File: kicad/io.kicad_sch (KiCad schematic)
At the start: 23 parts, among them J15 GPIO 5, J16 GPIO 6, J17 GPIO 20, J18 GPIO 21, J19 1-wire DS1820, J22 I2C 1, J23 I2C 2, J24 Display

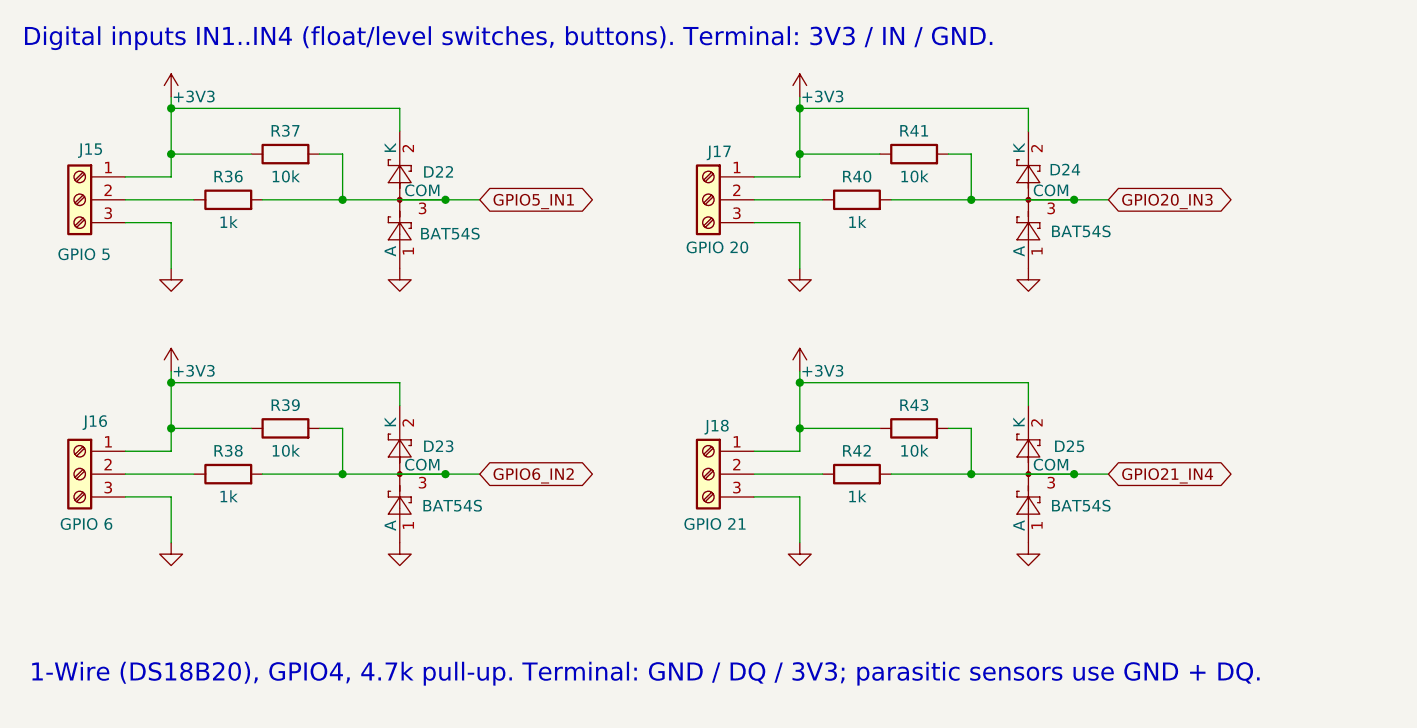
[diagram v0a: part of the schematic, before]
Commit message: kicad: strip obsolete v1 parts for v2 (SSR sheet, IN1..IN4, pH front end)
41 parts, their tracks/vias, pH guard zones, BNC keep-out and port silk removed; freed J2/U5 pins marked no-connect. ERC 0, DRC 0, parity 0; one expected +3V3 ratsnest to J24/JP3/J27/D28 left for the v2 layout.

Co-Authored-By: Claude Opus 5.5 <noreply@anthropic.com>
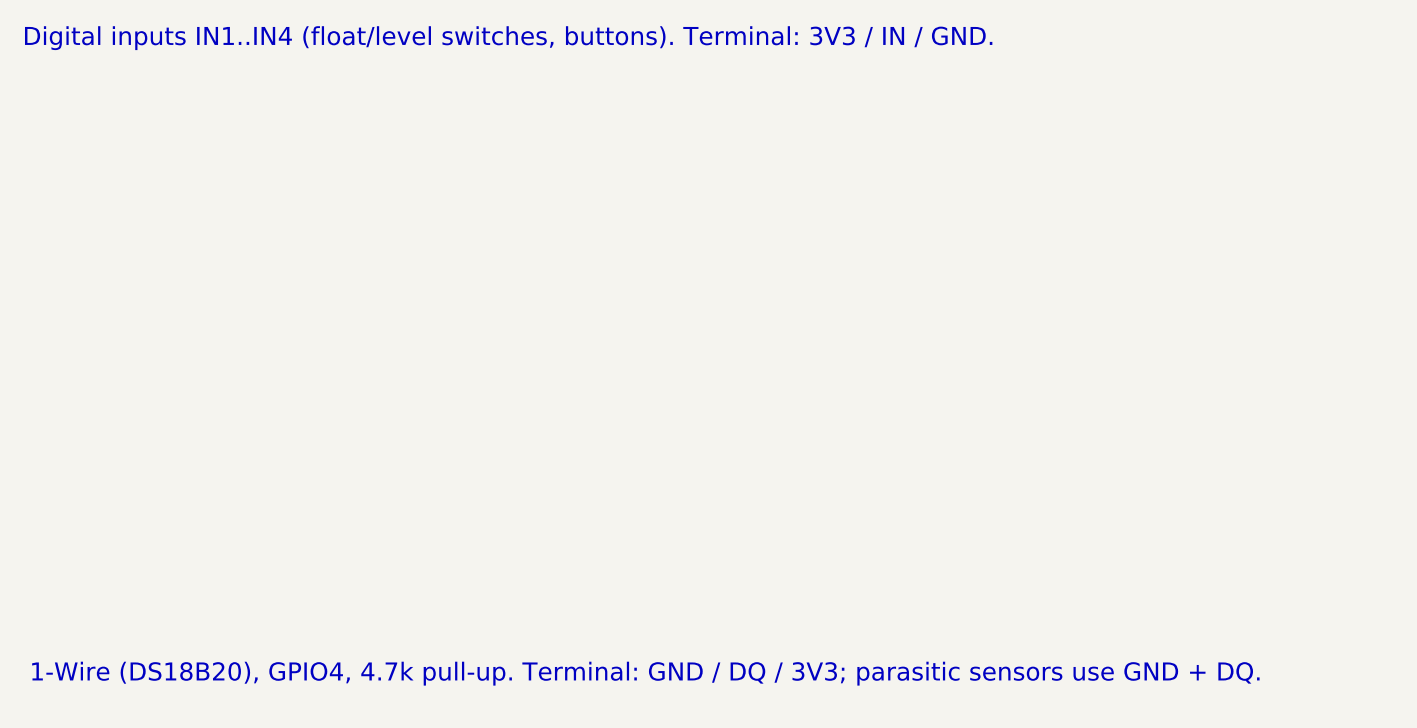
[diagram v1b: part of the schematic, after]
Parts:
- removed D22, D23, D24, D25: BAT54S, Package_TO_SOT_SMD:SOT-23, symbol Diode:BAT54S
- removed J15: GPIO 5, aquaPCB:TerminalBlock_Kangnex_WJ250B-3.5-03P_P3.50mm_Staggered, symbol Connector:Screw_Terminal_01x03
- removed J16: GPIO 6, aquaPCB:TerminalBlock_Kangnex_WJ250B-3.5-03P_P3.50mm_Staggered, symbol Connector:Screw_Terminal_01x03
- removed J17: GPIO 20, aquaPCB:TerminalBlock_Kangnex_WJ250B-3.5-03P_P3.50mm_Staggered, symbol Connector:Screw_Terminal_01x03
- removed J18: GPIO 21, aquaPCB:TerminalBlock_Kangnex_WJ250B-3.5-03P_P3.50mm_Staggered, symbol Connector:Screw_Terminal_01x03
- removed R36, R38, R40, R42: 1k, Resistor_SMD:R_0805_2012Metric, symbol Device:R
- removed R37, R39, R41, R43: 10k, Resistor_SMD:R_0805_2012Metric, symbol Device:R
